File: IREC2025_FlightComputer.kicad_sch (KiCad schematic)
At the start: 71 parts, among them J1 Molex Microfit, J2 BOOT0, J3 Companion, J5 SWD, Q1 SI7232DN-T1-GE3, U1 STM32U575VGTx, U5 LP5912Q3.3DRVRQ1, U8 TPS62153, U9 SN74HCT125DR, X1 1XXD32000MBA

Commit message: Chore: push new design
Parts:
- removed C2: 100nF, PCM_JLCPCB:C_0402, symbol PCM_JLCPCB-Capacitors:0402,100nF
- removed C3: 1uF, PCM_JLCPCB:C_0402, symbol PCM_JLCPCB-Capacitors:0402,1uF
- C1, C10, C11, C12, C13, C15, C16, C18, C22, C5, C6, C7, C70, C8, C9: footprint PCM_JLCPCB:C_0402 -> PCM_JLCPCB:C_0603
- C14: value 10nF -> 100nF; footprint PCM_JLCPCB:C_0402 -> PCM_JLCPCB:C_0603
- C20, C24, C4: footprint PCM_JLCPCB:C_0805 -> PCM_JLCPCB:C_0603
- C25: value GJM1555C1H3R3BB01D -> 3.3pF; footprint EasyEDA:C0402 -> PCM_JLCPCB:C_0603
- R16, R17: footprint PCM_JLCPCB:R_0402 -> PCM_JLCPCB:R_0603
- renumbered LED4 to PB0
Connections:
- net LORA_DIO3 renamed LORA_DIO1

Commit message: tung tung tung
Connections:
- net +5V: now also SERVO1.2 (Pin_2), SERVO2.2 (Pin_2); no longer SERVO1.1 (Pin_1), SERVO2.1 (Pin_1)
- net GND: now also SERVO1.3 (Pin_3), SERVO2.3 (Pin_3); no longer SERVO1.2 (Pin_2), SERVO2.2 (Pin_2)
- net SERVO_A: now also SERVO1.1 (Pin_1); no longer SERVO1.3 (Pin_3)
- net SERVO_B: now also SERVO2.1 (Pin_1); no longer SERVO2.3 (Pin_3)

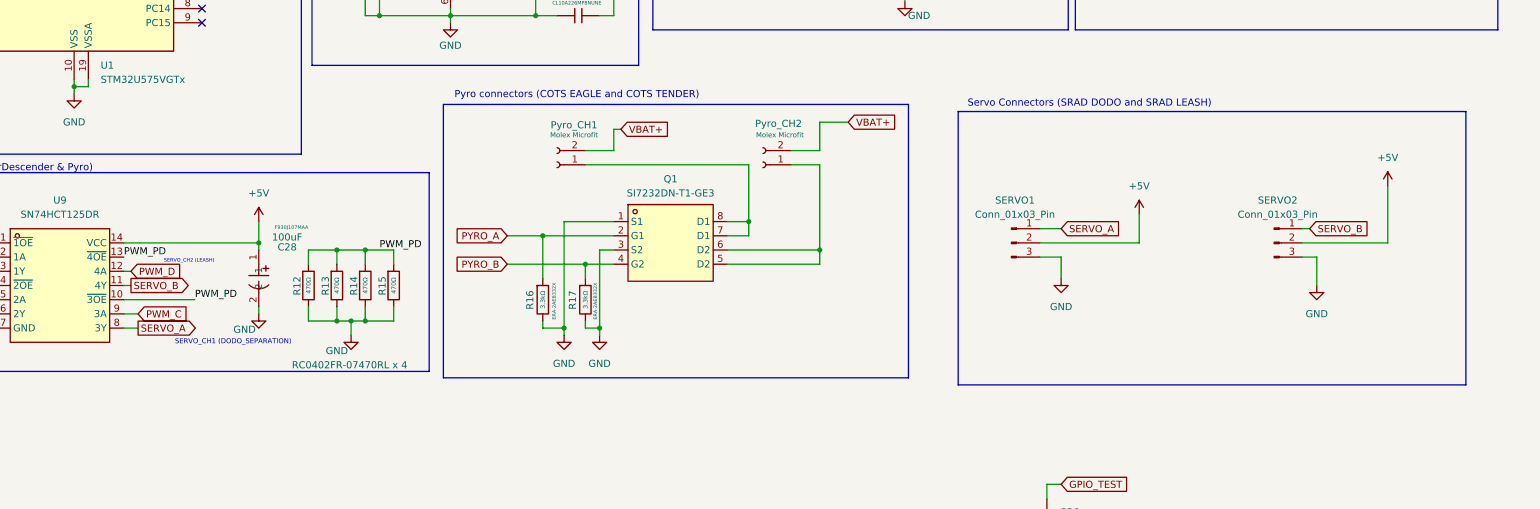
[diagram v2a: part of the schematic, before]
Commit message: Add current limit to servo
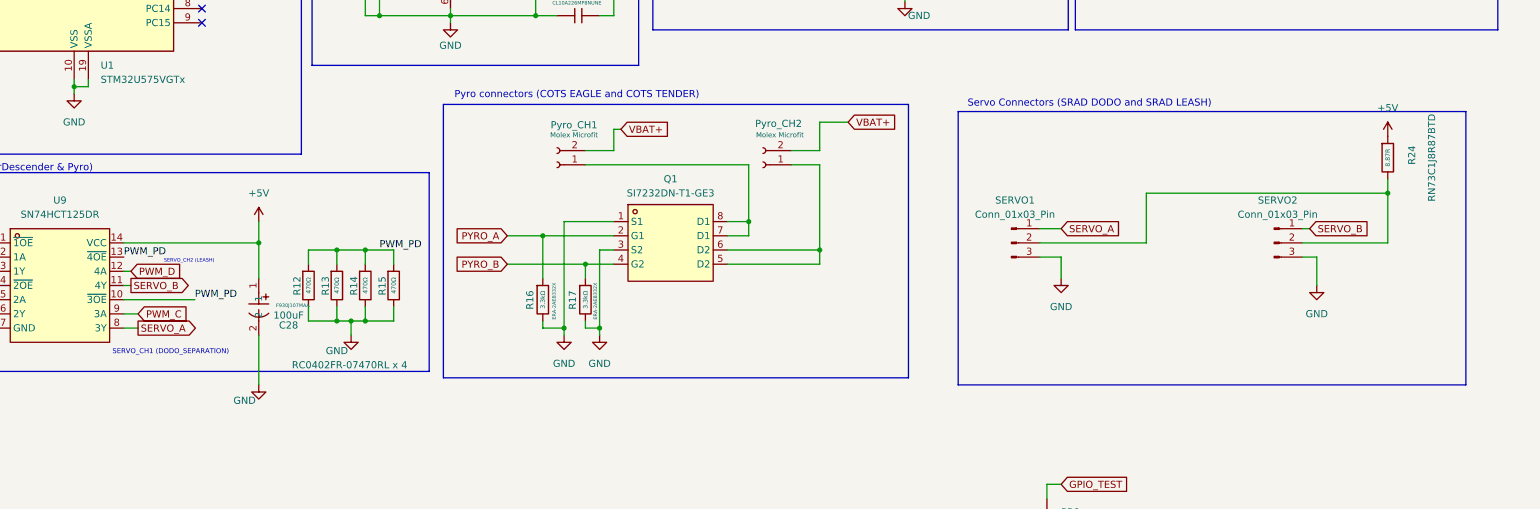
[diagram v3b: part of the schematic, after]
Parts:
- added R24: 8.87R, PCM_JLCPCB:R_0805, symbol PCM_JLCPCB-Resistors:0603,1kΩ
- FB1: footprint PCM_JLCPCB:FB_0805 -> PCM_JLCPCB:FB_0603
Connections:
- net +5V: now also R24.1; no longer SERVO1.2 (Pin_2), SERVO2.2 (Pin_2)
- new net: R24.2, SERVO1.2 (Pin_2), SERVO2.2 (Pin_2)
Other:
- moved on the sheet: C28

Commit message: Special version
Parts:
- added R23, R25: 5R, pyrolim:RES_3540_TEC, symbol PCM_JLCPCB-Resistors:0402,470Ω
- C1: Digikey Parts (none) -> 0603B101K500CT
- C10, C11, C13, C14, C17, C22, C5, C6, C7, C70, C8, C9: Digikey Parts (none) -> CL10B104KA8NNNC
- C12, C15, C16: Digikey Parts (none) -> CL10B105KO8NNNC
- C18, C20, C24, C4: Digikey Parts (none) -> CL10A106KP8NNNC
- C21: Digikey Parts (none) -> CL10B225KP8NNNC
- C23: Digikey Parts (none) -> CL10A226MP8NUNE
- C25: Digikey Parts (none) -> CL10C3R3CB81PNC
- C26: Digikey Parts (none) -> CL10A475MO8NNNC
- C28, C74: Digikey Parts (none) -> T55A107M007C0070
- R1, R38, R9: Digikey Parts (none) -> RC0603FR-0710KL
- R10: Digikey Parts (none) -> RC0603FR-07100KL
- R12, R13, R14, R15: Digikey Parts (none) -> RC0603JR-07470RL
- R16, R17: Digikey Parts (none) -> RMCF0603JT3K30
- R2: Digikey Parts (none) -> RC0603FR-0747KL
- R22, R39: Digikey Parts (none) -> RC0603JR-071KL
- R24: Digikey Parts (none) -> CRCW251220R0FKEG
- R3, R4: Digikey Parts (none) -> RC0603FR-075K1L
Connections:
- net VBAT+: now also R23.1, R25.1; no longer Pyro_CH1.2 (Pin_2), Pyro_CH2.2 (Pin_2)
- net at Q1.7 (D1), Q1.8 (D1): now also Pyro_CH2.1 (Pin_1); no longer Pyro_CH1.1 (Pin_1)
- net at Q1.5 (D2), Q1.6 (D2): now also Pyro_CH1.1 (Pin_1); no longer Pyro_CH2.1 (Pin_1)
- new net: Pyro_CH2.2 (Pin_2), R25.2
- new net: Pyro_CH1.2 (Pin_2), R23.2

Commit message: v2 manufactured ver.
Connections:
- net at Q1.5 (D2), Q1.6 (D2): now also Pyro_CH2.1 (Pin_1); no longer Pyro_CH1.1 (Pin_1)
- net at Q1.7 (D1), Q1.8 (D1): now also Pyro_CH1.1 (Pin_1); no longer Pyro_CH2.1 (Pin_1)
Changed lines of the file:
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@@
 	)
 	(junction
-		(at 203.2 203.2)
-		(diameter 0)
-		(color 0 0 0 0)
-	)
-	(junction
 		(at 200.66 198.12)
 		(diameter 0)
@@
 	)
 	(junction
+		(at 203.2 203.2)
+		(diameter 0)
+		(color 0 0 0 0)
+	)
+	(junction
 		(at 177.8 43.18)
 		(diameter 0)
@@
 	(wire
 		(pts
-			(xy 137.16 149.86) (xy 134.62 149.86)
+			(xy 208.28 187.96) (xy 208.28 203.2)
 		)
 		(stroke
@@
 	(wire
 		(pts
-			(xy 133.35 43.18) (xy 142.24 43.18)
+			(xy 137.16 149.86) (xy 134.62 149.86)
 		)
 		(stroke
@@
 	(wire
 		(pts
-			(xy 203.2 191.77) (xy 195.58 191.77)
+			(xy 133.35 43.18) (xy 142.24 43.18)
 		)
 		(stroke
@@
 	(wire
 		(pts
-			(xy 200.66 198.12) (xy 208.28 198.12)
-		)
-		(stroke
-			(width 0)
-			(type default)
-		)
-	)
-	(wire
-		(pts
 			(xy 54.61 116.84) (xy 57.15 116.84)
 		)
@@
 	(wire
 		(pts
-			(xy 208.28 198.12) (xy 208.28 187.96)
-		)
-		(stroke
-			(width 0)
-			(type default)
-		)
-	)
-	(wire
-		(pts
 			(xy 228.6 135.89) (xy 233.68 135.89)
 		)
@@
 	(wire
 		(pts
+			(xy 200.66 187.96) (xy 200.66 198.12)
+		)
+		(stroke
+			(width 0)
+			(type default)
+		)
+	)
+	(wire
+		(pts
 			(xy 160.02 74.93) (xy 168.91 74.93)
 		)
@@
 	(wire
 		(pts
+			(xy 203.2 203.2) (xy 208.28 203.2)
+		)
+		(stroke
+			(width 0)
+			(type default)
+		)
+	)
+	(wire
+		(pts
 			(xy 80.01 173.99) (xy 80.01 175.26)
 		)
@@
 	(wire
 		(pts
-			(xy 203.2 203.2) (xy 203.2 191.77)
-		)
-		(stroke
-			(width 0)
-			(type default)
-		)
-	)
-	(wire
-		(pts
 			(xy 171.45 217.17) (xy 173.99 217.17)
 		)
@@
 	(wire
 		(pts
-			(xy 195.58 191.77) (xy 195.58 187.96)
-		)
-		(stroke
-			(width 0)
-			(type default)
-		)
-	)
-	(wire
-		(pts
 			(xy 121.92 205.74) (xy 121.92 203.2)
 		)
@@
 	(wire
 		(pts
-			(xy 195.58 187.96) (xy 171.45 187.96)
+			(xy 171.45 187.96) (xy 200.66 187.96)
 		)
 		(stroke
